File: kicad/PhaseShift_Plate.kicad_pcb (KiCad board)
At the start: 2 copper layers, 66.4 x 128.6 mm, 0 parts

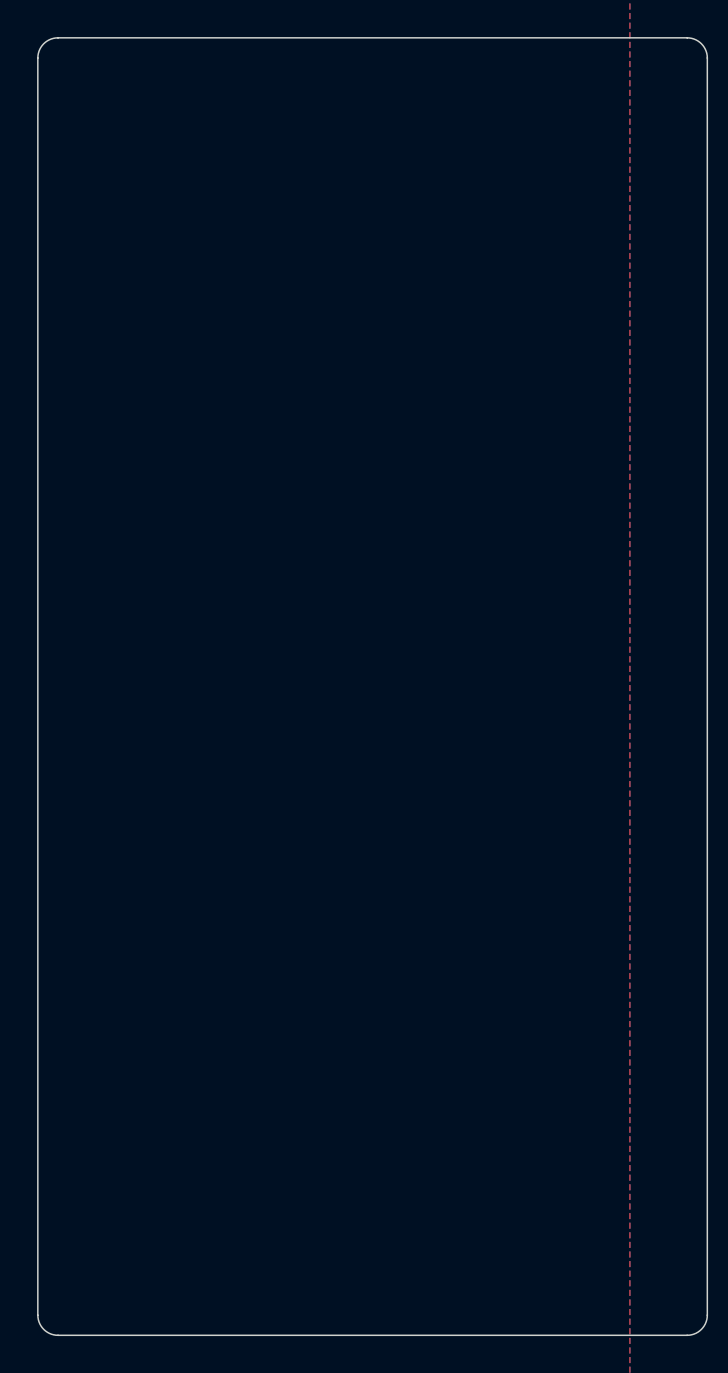
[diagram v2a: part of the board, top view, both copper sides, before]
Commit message: screw holes
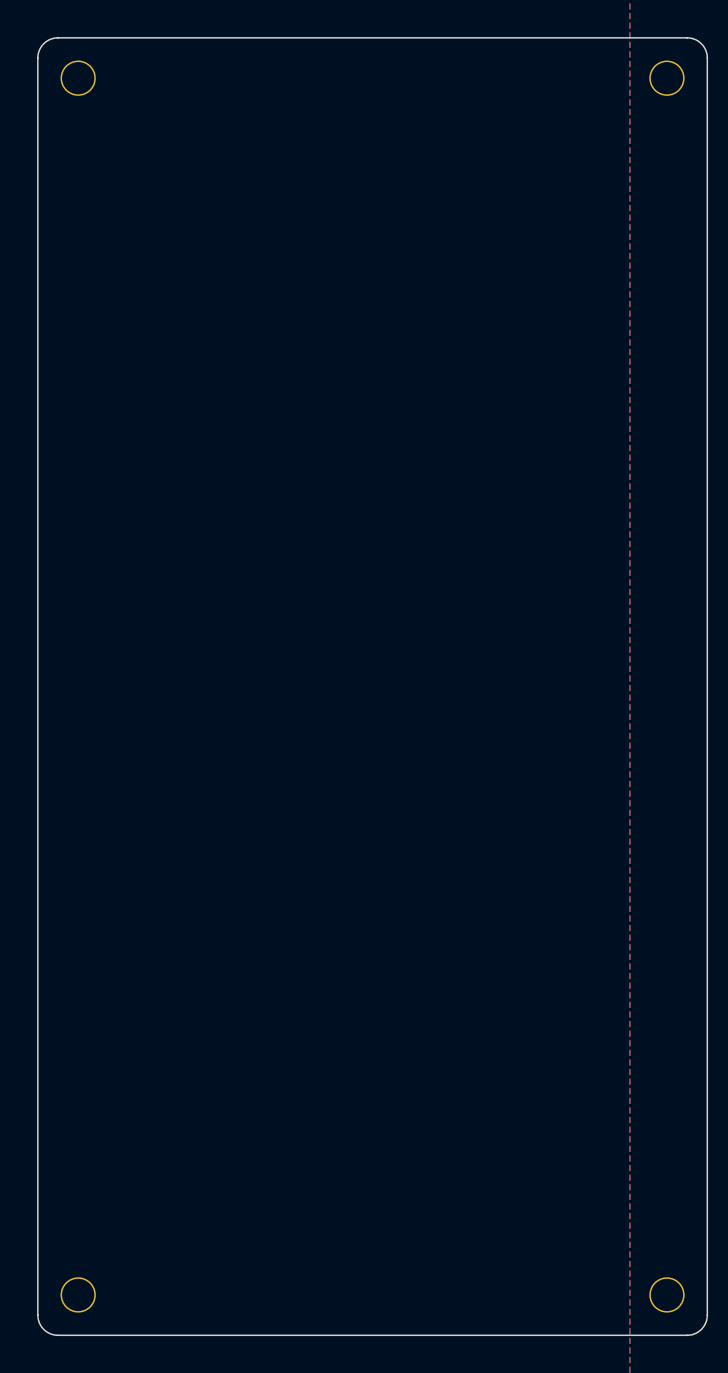
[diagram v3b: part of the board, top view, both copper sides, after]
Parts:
- added H1: MountingHole_3.2mm_Pad, TB2086_MISC:MountingHole_3.2mm_Pad, F.Cu at (365.3, 79.7)
- added H2: MountingHole_3.2mm_Pad, TB2086_MISC:MountingHole_3.2mm_Pad, F.Cu at (423.7, 79.7)
- added H3: MountingHole_3.2mm_Pad, TB2086_MISC:MountingHole_3.2mm_Pad, F.Cu at (423.7, 200.3)
- added H4: MountingHole_3.2mm_Pad, TB2086_MISC:MountingHole_3.2mm_Pad, F.Cu at (365.3, 200.3)
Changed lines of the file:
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@@
     (title "PhaseShift_Plate")
     (date "2025-07-03")
-    (rev "0.3.4")
+    (rev "0.3.5")
     (company "Allen Choi")
   )
@@
     )
   )
+(
+         footprint "TB2086_MISC:MountingHole_3.2mm_Pad"
+        (version 20241229)
+        (generator "pcbnew")
+        (generator_version "9.0")
+        (layer "F.Cu")
+        (descr "Mounting Hole 3.2mm, no annular, M3")
+        (tags "mounting hole 3.2mm no annular m3")
+        (property "Reference" "H1" (at 0 -4.2 0) (layer "F.SilkS") hide  (effects (font (size 1 1) (thickness 0.15))))
+        (attr exclude_from_pos_files exclude_from_bom)
+        (embedded_fonts no)
+        (at 365.32500000000005 79.7125 0)
+        (property "Value" "MountingHole_3.2mm_Pad" (at 0 4.2 0) (layer "F.Fab")  (effects (font (size 1 1) (thickness 0.15))))
+        (property "Datasheet" "" (at 0 0 0) (unlocked yes) (layer "F.Fab") (hide yes)  (effects (font (size 1.27 1.27) (thickness 0.15))))
+        (property "Description" "" (at 0 0 0) (unlocked yes) (layer "F.Fab") (hide yes)  (effects (font (size 1.27 1.27) (thickness 0.15))))
+        (fp_text user "${REFERENCE}" (at 0 0 0) (layer "F.Fab")  (effects (font (size 1 1) (thickness 0.15))))
+        (fp_circle (center 0 0) (end 3.45 0) (stroke (width 0.05) (type solid)) (fill no) (layer "F.CrtYd") )
+        (pad "1" thru_hole circle (at 0 0 0) (size 3.5 3.5) (drill 3.2) (layers "*.Cu" "*.Mask") (remove_unused_layers no) (zone_connect 2)  (net 1 "GND"))
+        (fp_circle (center 0 0) (end 3.2 0) (stroke (width 0.15) (type solid)) (fill no) (layer "Cmts.User") )
+            )
+(
+         footprint "TB2086_MISC:MountingHole_3.2mm_Pad"
+        (version 20241229)
+        (generator "pcbnew")
+        (generator_version "9.0")
+        (layer "F.Cu")
+        (descr "Mounting Hole 3.2mm, no annular, M3")
+        (tags "mounting hole 3.2mm no annular m3")
+        (property "Reference" "H2" (at 0 -4.2 0) (layer "F.SilkS") hide  (effects (font (size 1 1) (thickness 0.15))))
+        (attr exclude_from_pos_files exclude_from_bom)
+        (embedded_fonts no)
+        (at 423.67500000000007 79.7125 0)
+        (property "Value" "MountingHole_3.2mm_Pad" (at 0 4.2 0) (layer "F.Fab")  (effects (font (size 1 1) (thickness 0.15))))
+        (property "Datasheet" "" (at 0 0 0) (unlocked yes) (layer "F.Fab") (hide yes)  (effects (font (size 1.27 1.27) (thickness 0.15))))
+        (property "Description" "" (at 0 0 0) (unlocked yes) (layer "F.Fab") (hide yes)  (effects (font (size 1.27 1.27) (thickness 0.15))))
+        (fp_text user "${REFERENCE}" (at 0 0 0) (layer "F.Fab")  (effects (font (size 1 1) (thickness 0.15))))
+        (fp_circle (center 0 0) (end 3.45 0) (stroke (width 0.05) (type solid)) (fill no) (layer "F.CrtYd") )
+        (pad "1" thru_hole circle (at 0 0 0) (size 3.5 3.5) (drill 3.2) (layers "*.Cu" "*.Mask") (remove_unused_layers no) (zone_connect 2)  (net 1 "GND"))
+        (fp_circle (center 0 0) (end 3.2 0) (stroke (width 0.15) (type solid)) (fill no) (layer "Cmts.User") )
+            )
+(
+         footprint "TB2086_MISC:MountingHole_3.2mm_Pad"
+        (version 20241229)
+        (generator "pcbnew")
+        (generator_version "9.0")
+        (layer "F.Cu")
+        (descr "Mounting Hole 3.2mm, no annular, M3")
+        (tags "mounting hole 3.2mm no annular m3")
+        (property "Reference" "H3" (at 0 -4.2 0) (layer "F.SilkS") hide  (effects (font (size 1 1) (thickness 0.15))))
+        (attr exclude_from_pos_files exclude_from_bom)
+        (embedded_fonts no)
+        (at 423.67500000000007 200.29999999999998 0)
+        (property "Value" "MountingHole_3.2mm_Pad" (at 0 4.2 0) (layer "F.Fab")  (effects (font (size 1 1) (thickness 0.15))))
+        (property "Datasheet" "" (at 0 0 0) (unlocked yes) (layer "F.Fab") (hide yes)  (effects (font (size 1.27 1.27) (thickness 0.15))))
+        (property "Description" "" (at 0 0 0) (unlocked yes) (layer "F.Fab") (hide yes)  (effects (font (size 1.27 1.27) (thickness 0.15))))
+        (fp_text user "${REFERENCE}" (at 0 0 0) (layer "F.Fab")  (effects (font (size 1 1) (thickness 0.15))))
+        (fp_circle (center 0 0) (end 3.45 0) (stroke (width 0.05) (type solid)) (fill no) (layer "F.CrtYd") )
+        (pad "1" thru_hole circle (at 0 0 0) (size 3.5 3.5) (drill 3.2) (layers "*.Cu" "*.Mask") (remove_unused_layers no) (zone_connect 2)  (net 1 "GND"))
+        (fp_circle (center 0 0) (end 3.2 0) (stroke (width 0.15) (type solid)) (fill no) (layer "Cmts.User") )
+            )
+(
+         footprint "TB2086_MISC:MountingHole_3.2mm_Pad"
+        (version 20241229)
+        (generator "pcbnew")
+        (generator_version "9.0")
+        (layer "F.Cu")
+        (descr "Mounting Hole 3.2mm, no annular, M3")
+        (tags "mounting hole 3.2mm no annular m3")
+        (property "Reference" "H4" (at 0 -4.2 0) (layer "F.SilkS") hide  (effects (font (size 1 1) (thickness 0.15))))
+        (attr exclude_from_pos_files exclude_from_bom)
+        (embedded_fonts no)
+        (at 365.32500000000005 200.29999999999998 0)
+        (property "Value" "MountingHole_3.2mm_Pad" (at 0 4.2 0) (layer "F.Fab")  (effects (font (size 1 1) (thickness 0.15))))
+        (property "Datasheet" "" (at 0 0 0) (unlocked yes) (layer "F.Fab") (hide yes)  (effects (font (size 1.27 1.27) (thickness 0.15))))
+        (property "Description" "" (at 0 0 0) (unlocked yes) (layer "F.Fab") (hide yes)  (effects (font (size 1.27 1.27) (thickness 0.15))))
+        (fp_text user "${REFERENCE}" (at 0 0 0) (layer "F.Fab")  (effects (font (size 1 1) (thickness 0.15))))
+        (fp_circle (center 0 0) (end 3.45 0) (stroke (width 0.05) (type solid)) (fill no) (layer "F.CrtYd") )
+        (pad "1" thru_hole circle (at 0 0 0) (size 3.5 3.5) (drill 3.2) (layers "*.Cu" "*.Mask") (remove_unused_layers no) (zone_connect 2)  (net 1 "GND"))
+        (fp_circle (center 0 0) (end 3.2 0) (stroke (width 0.15) (type solid)) (fill no) (layer "Cmts.User") )
+            )
   (gr_line (start 361.32500000000005 202.29999999999998) (end 361.32500000000005 77.7125) (layer Edge.Cuts) (stroke (width 0.15) (type default)))
 (gr_line (start 363.32500000000005 75.7125) (end 425.67500000000007 75.7125) (layer Edge.Cuts) (stroke (width 0.15) (type default)))

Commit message: pogo pin - ergogen
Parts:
- moved H1 190.0 mm to (175.3, 79.7)
- moved H2 190.0 mm to (233.7, 79.7)
- moved H3 190.0 mm to (233.7, 200.3)
- moved H4 190.0 mm to (175.3, 200.3)

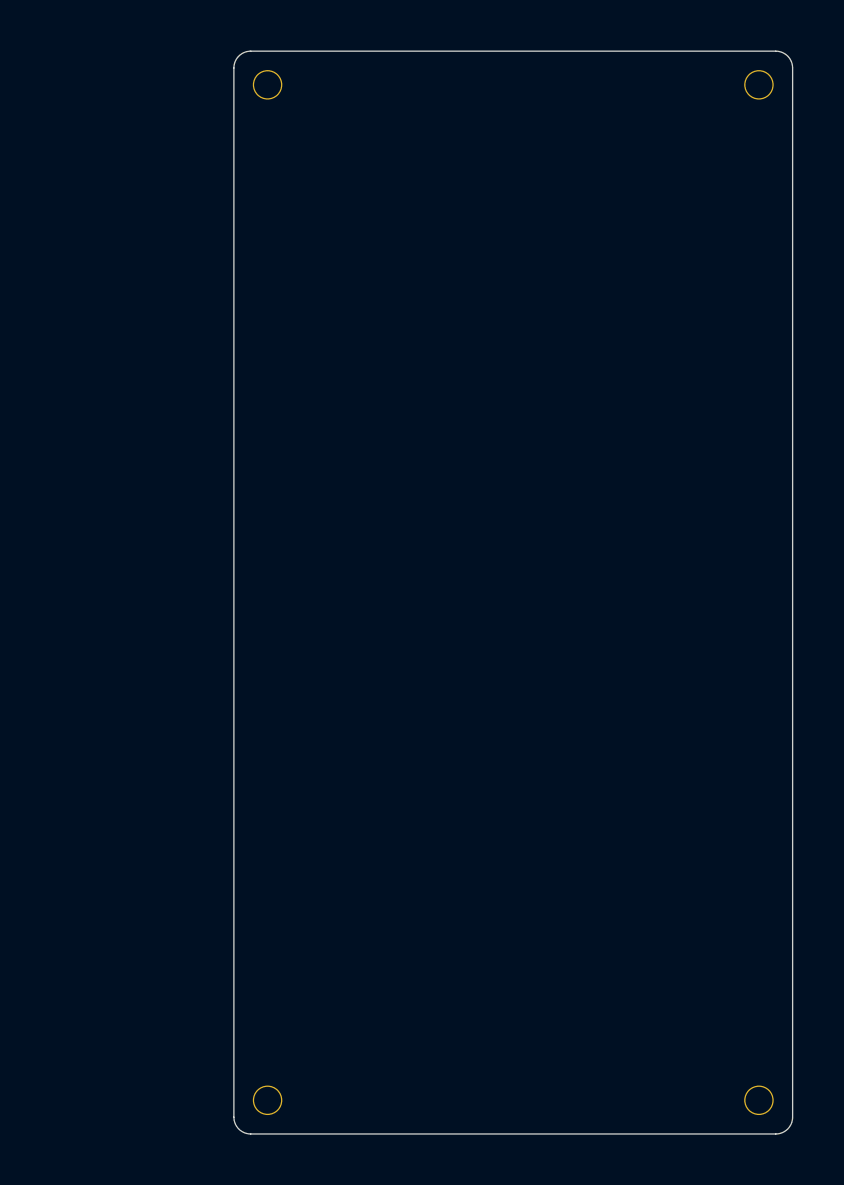
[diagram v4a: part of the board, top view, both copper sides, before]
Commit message: changed screw sizes
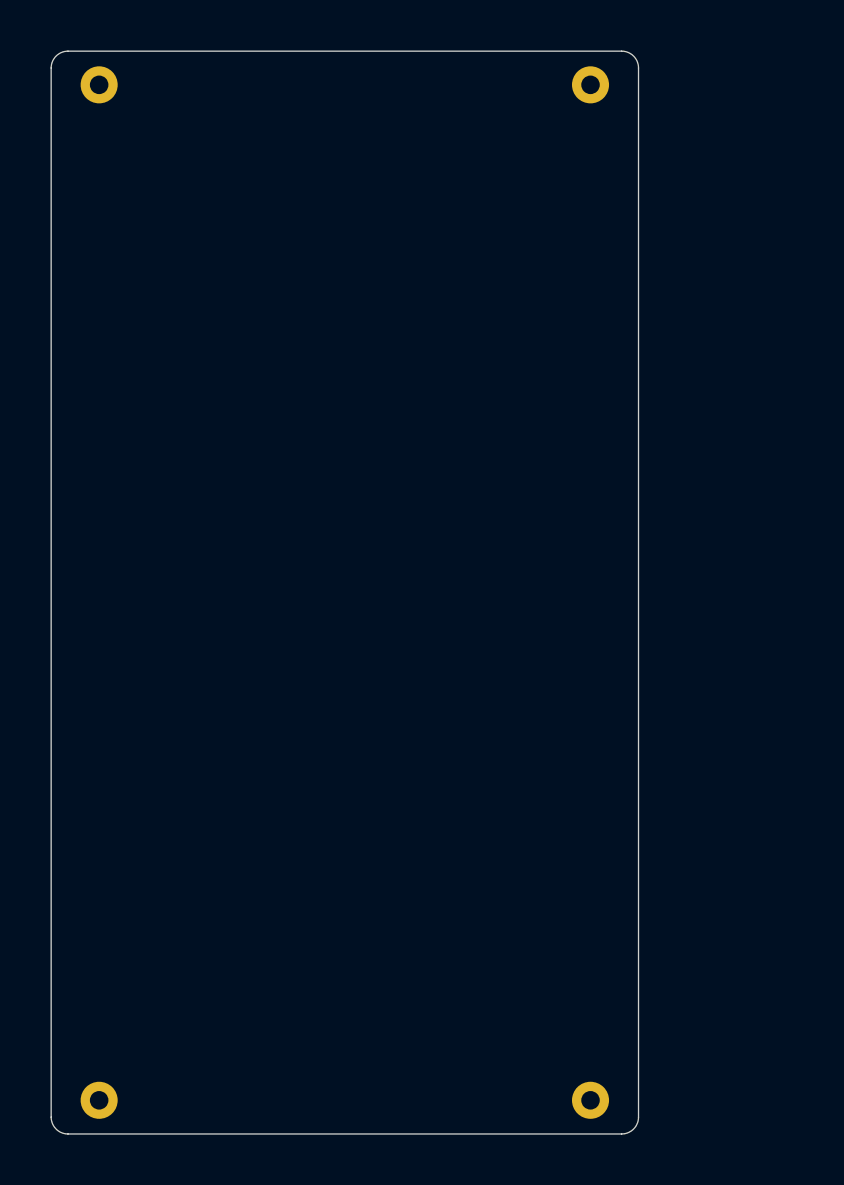
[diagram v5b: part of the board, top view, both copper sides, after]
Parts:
- H1, H2, H3, H4: value MountingHole_3.2mm_Pad -> MountingHole_2.2mm_M2_Pad; footprint TB2086_MISC:MountingHole_3.2mm_Pad -> TB2086_MISC:MountingHole_2.2mm_M2_Pad
- moved H1 20.0 mm to (155.3, 79.7)
- moved H2 20.0 mm to (213.7, 79.7)
- moved H3 20.0 mm to (213.7, 200.3)
- moved H4 20.0 mm to (155.3, 200.3)
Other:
- board size 66.4 x 128.6 mm -> 69.8 x 128.6 mm
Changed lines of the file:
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@@
 	(title_block
 		(title "PhaseShift_Plate")
-		(date "2025-07-04")
-		(rev "0.3.6")
+		(date "2025-07-08")
+		(rev "0.4.3")
 		(company "Allen Choi")
 	)
@@
 	(net 0 "")
 	(net 1 "GND")
-	(footprint "TB2086_MISC:MountingHole_3.2mm_Pad"
+	(footprint "TB2086_MISC:MountingHole_2.2mm_M2_Pad"
 		(layer "F.Cu")
-		(at 233.675 79.7125)
-		(descr "Mounting Hole 3.2mm, no annular, M3")
-		(tags "mounting hole 3.2mm no annular m3")
-		(property "Reference" "H2"
-			(at 0 -4.2 0)
+		(at 213.675 200.3)
+		(descr "Mounting Hole 2.2mm, M2")
+		(tags "mounting hole 2.2mm m2")
+		(property "Reference" "H3"
+			(at 0 -3.2 0)
 			(layer "F.SilkS")
 			(hide yes)
@@
 			)
 		)
-		(property "Value" "MountingHole_3.2mm_Pad"
-			(at 0 4.2 0)
+		(property "Value" "MountingHole_2.2mm_M2_Pad"
+			(at 0 3.2 0)
 			(layer "F.Fab")
 			(effects
@@
 		(fp_circle
 			(center 0 0)
-			(end 3.2 0)
+			(end 2.2 0)
 			(stroke
 				(width 0.15)
@@
 		(fp_circle
 			(center 0 0)
-			(end 3.45 0)
+			(end 2.45 0)
 			(stroke
 				(width 0.05)
@@
 		(pad "1" thru_hole circle
 			(at 0 0)
-			(size 3.5 3.5)
-			(drill 3.2)
+			(size 4.4 4.4)
+			(drill 2.2)
 			(layers "*.Cu" "*.Mask")
 			(remove_unused_layers no)
 			(net 1 "GND")
-			(zone_connect 2)
 		)
 		(embedded_fonts no)
 	)
-	(footprint "TB2086_MISC:MountingHole_3.2mm_Pad"
+	(footprint "TB2086_MISC:MountingHole_2.2mm_M2_Pad"
 		(layer "F.Cu")
-		(at 175.325 79.7125)
-		(descr "Mounting Hole 3.2mm, no annular, M3")
-		(tags "mounting hole 3.2mm no annular m3")
+		(at 155.325 79.7125)
+		(descr "Mounting Hole 2.2mm, M2")
+		(tags "mounting hole 2.2mm m2")
 		(property "Reference" "H1"
-			(at 0 -4.2 0)
+			(at 0 -3.2 0)
 			(layer "F.SilkS")
 			(hide yes)
@@
 			)
 		)
-		(property "Value" "MountingHole_3.2mm_Pad"
-			(at 0 4.2 0)
+		(property "Value" "MountingHole_2.2mm_M2_Pad"
+			(at 0 3.2 0)
 			(layer "F.Fab")
 			(effects
@@
 		(fp_circle
 			(center 0 0)
-			(end 3.2 0)
+			(end 2.2 0)
 			(stroke
 				(width 0.15)
@@
 		(fp_circle
 			(center 0 0)
-			(end 3.45 0)
+			(end 2.45 0)
 			(stroke
 				(width 0.05)
@@
 		(pad "1" thru_hole circle
 			(at 0 0)
-			(size 3.5 3.5)
-			(drill 3.2)
+			(size 4.4 4.4)
+			(drill 2.2)
 			(layers "*.Cu" "*.Mask")
 			(remove_unused_layers no)
 			(net 1 "GND")
-			(zone_connect 2)
 		)
 		(embedded_fonts no)
 	)
-	(footprint "TB2086_MISC:MountingHole_3.2mm_Pad"
+	(footprint "TB2086_MISC:MountingHole_2.2mm_M2_Pad"
 		(layer "F.Cu")
-		(at 175.325 200.3)
-		(descr "Mounting Hole 3.2mm, no annular, M3")
-		(tags "mounting hole 3.2mm no annular m3")
-		(property "Reference" "H4"
-			(at 0 -4.2 0)
+		(at 213.675 79.7125)
+		(descr "Mounting Hole 2.2mm, M2")
+		(tags "mounting hole 2.2mm m2")
+		(property "Reference" "H2"
+			(at 0 -3.2 0)
 			(layer "F.SilkS")
 			(hide yes)
@@
 			)
 		)
-		(property "Value" "MountingHole_3.2mm_Pad"
-			(at 0 4.2 0)
+		(property "Value" "MountingHole_2.2mm_M2_Pad"
+			(at 0 3.2 0)
 			(layer "F.Fab")
 			(effects
@@
 		(fp_circle
 			(center 0 0)
-			(end 3.2 0)
+			(end 2.2 0)
 			(stroke
 				(width 0.15)
@@
 		(fp_circle
 			(center 0 0)
-			(end 3.45 0)
+			(end 2.45 0)
 			(stroke
 				(width 0.05)
@@
 		(pad "1" thru_hole circle
 			(at 0 0)
-			(size 3.5 3.5)
-			(drill 3.2)
+			(size 4.4 4.4)
+			(drill 2.2)
 			(layers "*.Cu" "*.Mask")
 			(remove_unused_layers no)
 			(net 1 "GND")
-			(zone_connect 2)
 		)
 		(embedded_fonts no)
 	)
-	(footprint "TB2086_MISC:MountingHole_3.2mm_Pad"
+	(footprint "TB2086_MISC:MountingHole_2.2mm_M2_Pad"
 		(layer "F.Cu")
-		(at 233.675 200.3)
-		(descr "Mounting Hole 3.2mm, no annular, M3")
-		(tags "mounting hole 3.2mm no annular m3")
-		(property "Reference" "H3"
-			(at 0 -4.2 0)
+		(at 155.325 200.3)
+		(descr "Mounting Hole 2.2mm, M2")
+		(tags "mounting hole 2.2mm m2")
+		(property "Reference" "H4"
+			(at 0 -3.2 0)
 			(layer "F.SilkS")
 			(hide yes)
@@
 			)
 		)
-		(property "Value" "MountingHole_3.2mm_Pad"
-			(at 0 4.2 0)
+		(property "Value" "MountingHole_2.2mm_M2_Pad"
+			(at 0 3.2 0)
 			(layer "F.Fab")
 			(effects
@@
 		(fp_circle
 			(center 0 0)
-			(end 3.2 0)
+			(end 2.2 0)
 			(stroke
 				(width 0.15)
@@
 		(fp_circle
 			(center 0 0)
-			(end 3.45 0)
+			(end 2.45 0)
 			(stroke
 				(width 0.05)
@@
 		(pad "1" thru_hole circle
 			(at 0 0)
-			(size 3.5 3.5)
-			(drill 3.2)
+			(size 4.4 4.4)
+			(drill 2.2)
 			(layers "*.Cu" "*.Mask")
 			(remove_unused_layers no)
 			(net 1 "GND")
-			(zone_connect 2)
 		)
 		(embedded_fonts no)
 	)
+	(gr_arc
+		(start 151.625 204.3)
+		(mid 150.210786 203.714214)
+		(end 149.625 202.3)
+		(stroke
+			(width 0.15)
+			(type default)
+		)
+		(layer "Edge.Cuts")
+	)
 	(gr_line
-		(start 171.325 202.3)
-		(end 171.325 77.7125)
+		(start 151.625 75.7125)
+		(end 217.375 75.7125)
 		(stroke
 			(width 0.15)
@@
 	)
 	(gr_line
-		(start 173.325 75.7125)
-		(end 235.675 75.7125)
+		(start 149.625 202.3)
+		(end 149.625 77.7125)
+		(stroke
+			(width 0.15)
+			(type default)
+		)
+		(layer "Edge.Cuts")
+	)
+	(gr_line
+		(start 219.375 77.7125)
+		(end 219.375 202.3)
 		(stroke
 			(width 0.15)
@@
 	)
 	(gr_arc
-		(start 171.325 77.7125)
-		(mid 171.910786 76.298286)
-		(end 173.325 75.7125)
+		(start 219.375 202.3)
+		(mid 218.789214 203.714214)
+		(end 217.375 204.3)
+		(stroke
+			(width 0.15)
+			(type default)
+		)
+		(layer "Edge.Cuts")
+	)
+	(gr_arc
+		(start 149.625 77.7125)
+		(mid 150.210786 76.298286)
+		(end 151.625 75.7125)
 		(stroke
 			(width 0.15)
@@
 	)
 	(gr_line
-		(start 235.675 204.3)
-		(end 173.325 204.3)
+		(start 217.375 204.3)
+		(end 151.625 204.3)
 		(stroke
 			(width 0.15)
@@
 	)
 	(gr_arc
-		(start 237.675 202.3)
-		(mid 237.089214 203.714214)
-		(end 235.675 204.3)
-		(stroke
-			(width 0.15)
-			(type default)
-		)
-		(layer "Edge.Cuts")
-	)
-	(gr_line
-		(start 237.675 77.7125)
-		(end 237.675 202.3)
-		(stroke
-			(width 0.15)
-			(type default)
-		)
-		(layer "Edge.Cuts")
-	)
-	(gr_arc
-		(start 235.675 75.7125)
-		(mid 237.089214 76.298286)
-		(end 237.675 77.7125)
-		(stroke
-			(width 0.15)
-			(type default)
-		)
-		(layer "Edge.Cuts")
-	)
-	(gr_arc
-		(start 173.325 204.3)
-		(mid 171.910786 203.714214)
-		(end 171.325 202.3)
-		(stroke
-			(width 0.15)
+		(start 217.375 75.7125)
+		(mid 218.789214 76.298286)
+		(end 219.375 77.7125)
+		(stroke
+			(width 0.15)

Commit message: fixed positions for screw holes
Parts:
- moved H1 211.0 mm to (366.3, 80.7)
- moved H4 211.0 mm to (366.3, 199.3)
- moved H2 209.0 mm to (422.7, 80.7)
- moved H3 209.0 mm to (422.7, 199.3)

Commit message: more tweaks  (#3)
* small tweaks

* GlyphMatrix - 3mm screws

* PhaseShift - 3mm screws

* DeltaForm - 3mm screws

* updated README.md
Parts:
- H1, H2, H3, H4: value MountingHole_2.2mm_M2_Pad -> MountingHole_3.2mm_Pad; footprint TB2086_MISC:MountingHole_2.2mm_M2_Pad -> TB2086_MISC:MountingHole_3.2mm_Pad
- moved H1 210.5 mm to (155.8, 80.2)
- moved H4 210.5 mm to (155.8, 199.8)
- moved H2 209.5 mm to (213.2, 80.2)
- moved H3 209.5 mm to (213.2, 199.8)

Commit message: plates (#4)
* Silk Screen

* small changes for GlyphMatrix

* Silk screen for plates

* amended GlyphMatrix
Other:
- board text added: "PhaseShift"
